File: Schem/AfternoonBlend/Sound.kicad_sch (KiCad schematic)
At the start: 56 parts, among them J4 STX-3120-3B, J5 Conn_01x03, U10 LM4880MX/NOPB, U11 SN76489AN, U12 SN76489AN, U2 TLV2372, U3 AD7801BRUZ, U6 SN76489AN, U7 SN76489AN, U8 74HC138, U9 74HCT21, Y1 ECS-2100A-035

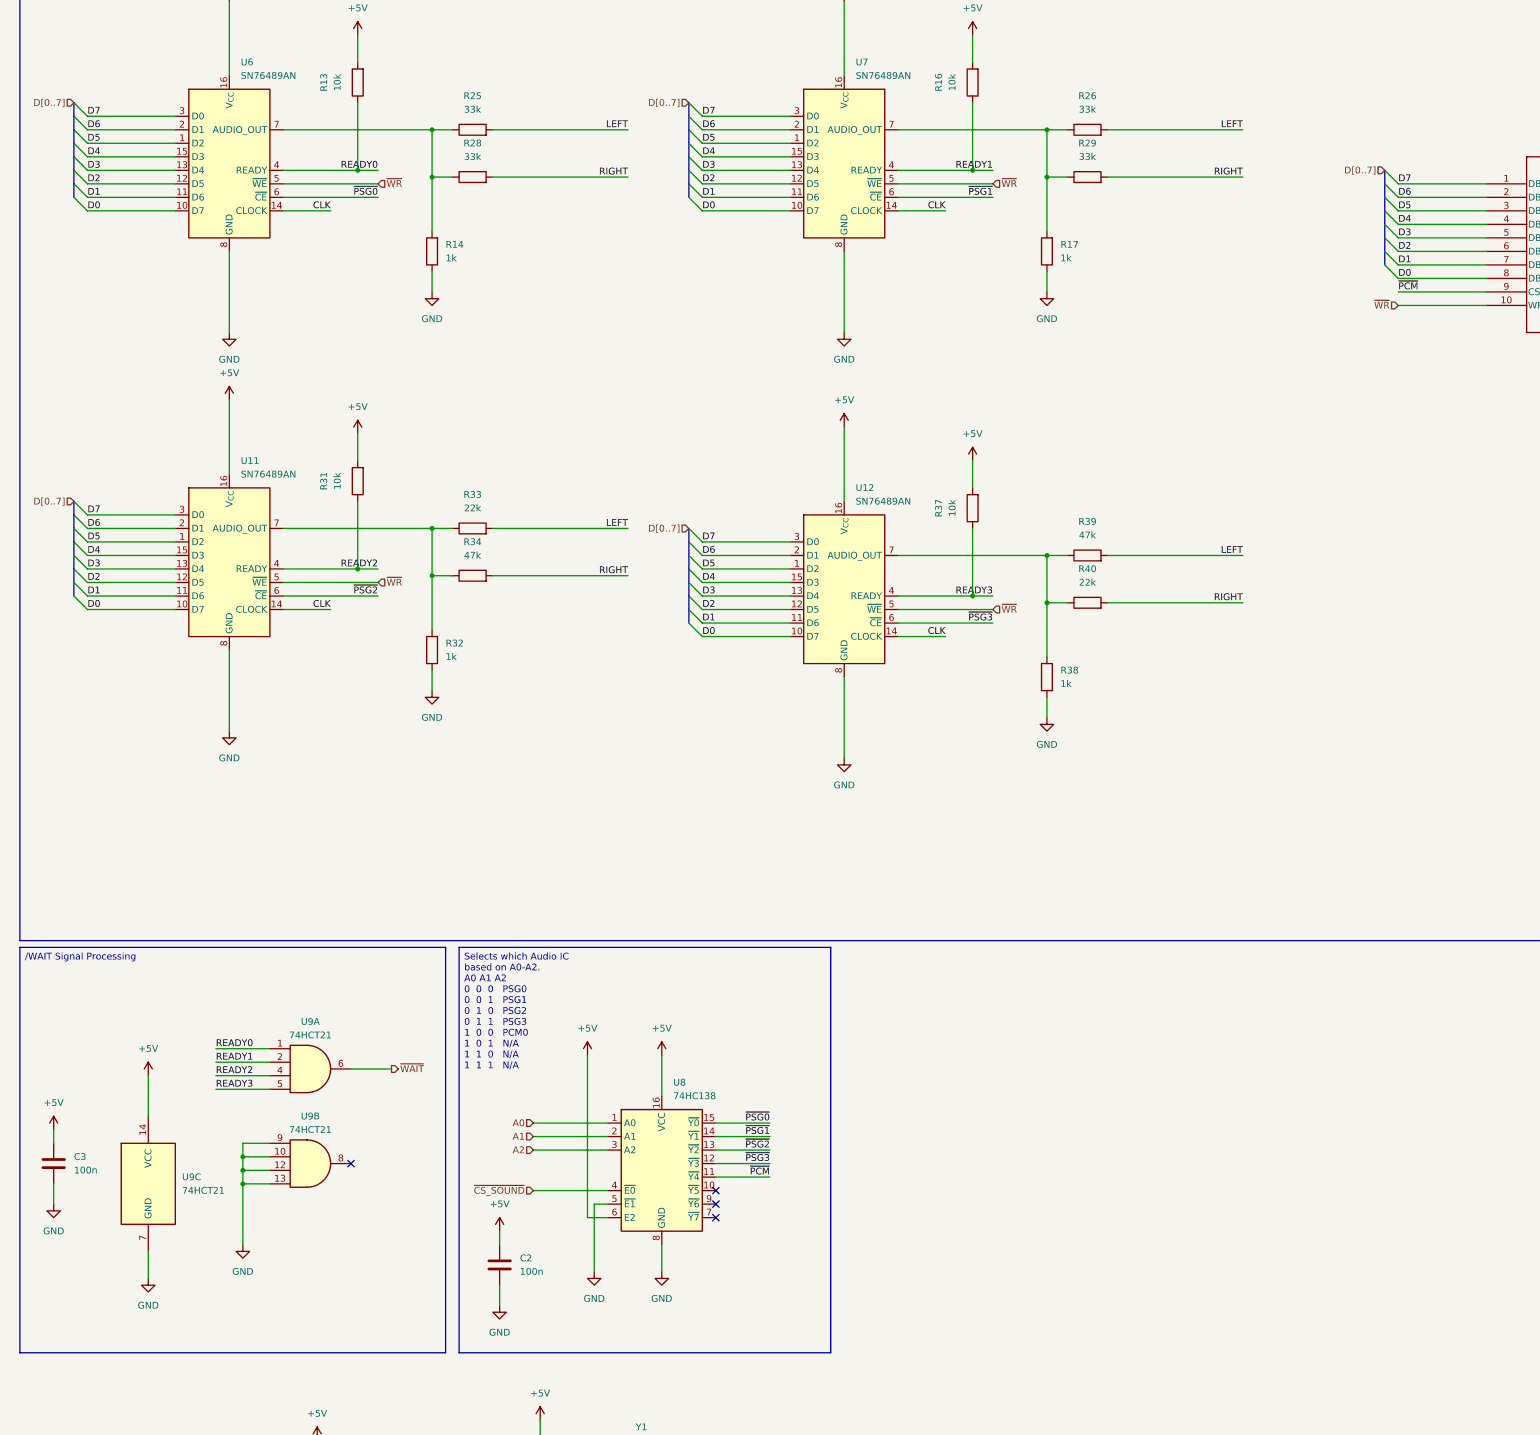
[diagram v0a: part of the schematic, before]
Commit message: Added a buffer on the Data Line to avoid overloading the CPU data bus with the 5 ICs on the board.
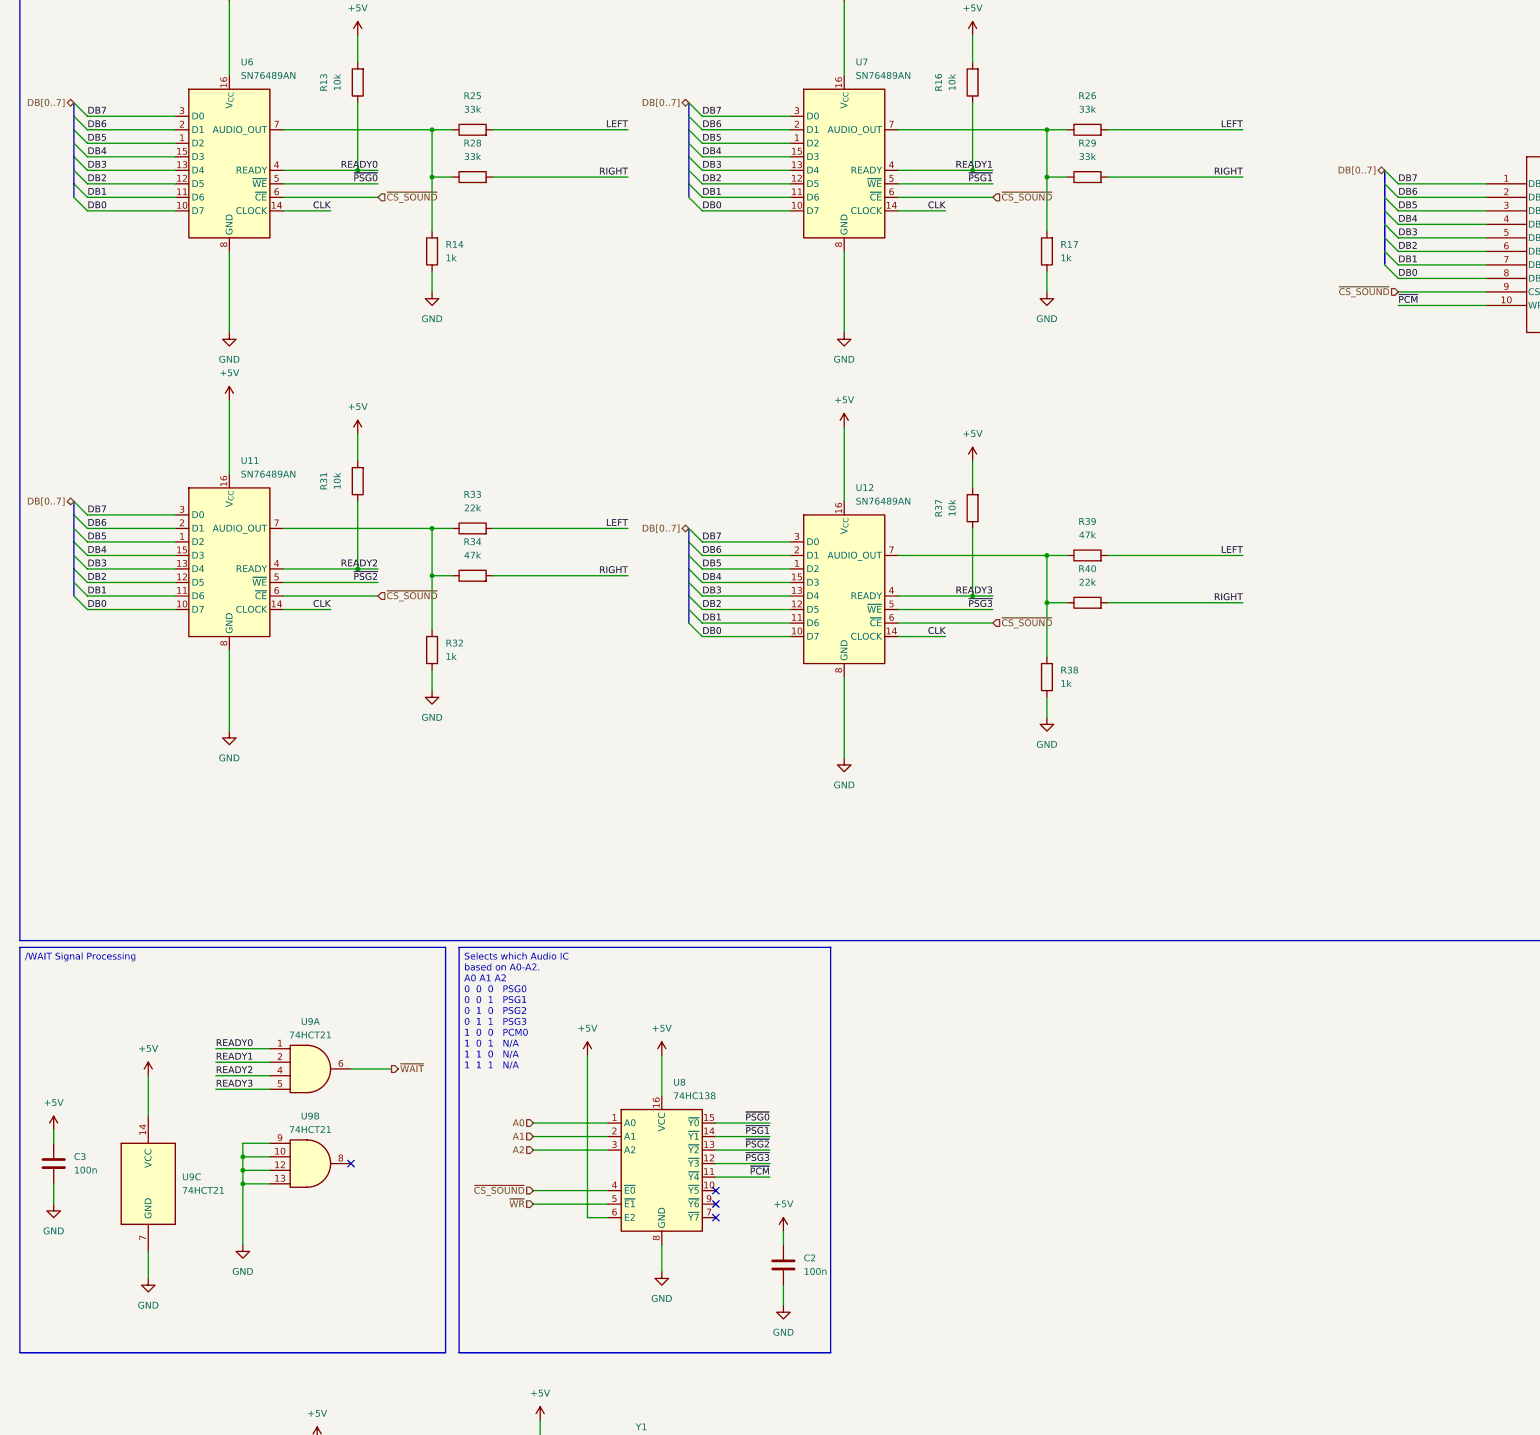
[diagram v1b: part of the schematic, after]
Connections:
- net GND: no longer U8.5 (~{E1})
- net ~{CS_SOUND}: now also U11.6 (~{CE}), U12.6 (~{CE}), U3.9 (CS*), U6.6 (~{CE}), U7.6 (~{CE})
- net ~{PCM}: now also U3.10 (WR*); no longer U3.9 (CS*)
- net ~{PSG0}: now also U6.5 (~{WE}); no longer U6.6 (~{CE})
- net ~{PSG1}: now also U7.5 (~{WE}); no longer U7.6 (~{CE})
- net ~{PSG2}: now also U11.5 (~{WE}); no longer U11.6 (~{CE})
- net ~{PSG3}: now also U12.5 (~{WE}); no longer U12.6 (~{CE})
- net ~{WR}: now also U8.5 (~{E1}); no longer U11.5 (~{WE}), U12.5 (~{WE}), U3.10 (WR*), U6.5 (~{WE}), U7.5 (~{WE})
- net D0 renamed DB0
- net D1 renamed DB1
- net D2 renamed DB2
- net D3 renamed DB3
- net D4 renamed DB4
- net D5 renamed DB5
- net D6 renamed DB6
- net D7 renamed DB7
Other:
- moved on the sheet: C2
